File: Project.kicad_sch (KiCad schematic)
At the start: 0 parts

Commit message: 修复晶振画错了的问题
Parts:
- added C1, C2: 1uF, symbol Lib1:C(MM)-LibCool
- added C3: 10uF, symbol Lib1:C(MM)-LibCool
- added C4, C5: 18pF, symbol Lib1:C(MM)-LibCool
- added F1: 20A, symbol Lib1:FUSE*-LibCool
- added P1: USB_C_Plug, symbol Connector:USB_C_Plug
- added R?: 1M, symbol Lib1:RES(M)-LibCool
- added SW1: DOUBLE_KEY, symbol Lib1:DOUBLE_KEY
- added U1: MAX15062A, Package_DFN_QFN:DFN-8_2x2mm_P0.5mm, symbol Regulator_Switching:MAX15062A
- added U2: TUSB8041, Package_DFN_QFN:QFN-64-1EP_9x9mm_P0.5mm_EP6x6mm_ThermalVias, symbol Interface_USB:TUSB8041
- added Y1: 24MHz, symbol Lib1:OSC-LibCool
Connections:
- new net: C2.1, F1.1, P1.A4 (VBUS), P1.A9 (VBUS), P1.B4 (VBUS), P1.B9 (VBUS)
- new net: C1.1, U1.3 (VCC)
- new net: C4.2, R?.2, U2.62 (XI), Y1.1
- new net: C5.2, R?.1, U2.61 (XO), Y1.2
- new net: P1.A1 (GND), P1.A12 (GND), P1.B1 (GND), P1.B12 (GND)
- new net: SW1.1, U2.50 (GRSTz)
- new net +3V3: C3.1, SW1.2, U1.4 (FB/Vout)
- new net GND: C1.2, C2.2, C3.2, C4.1, C5.1, SW1.2, U1.7 (GND)
- new net POWER: F1.2, U1.1 (VIN), U1.2 (EN/UVLO), U2.48 (USB_VBUS)

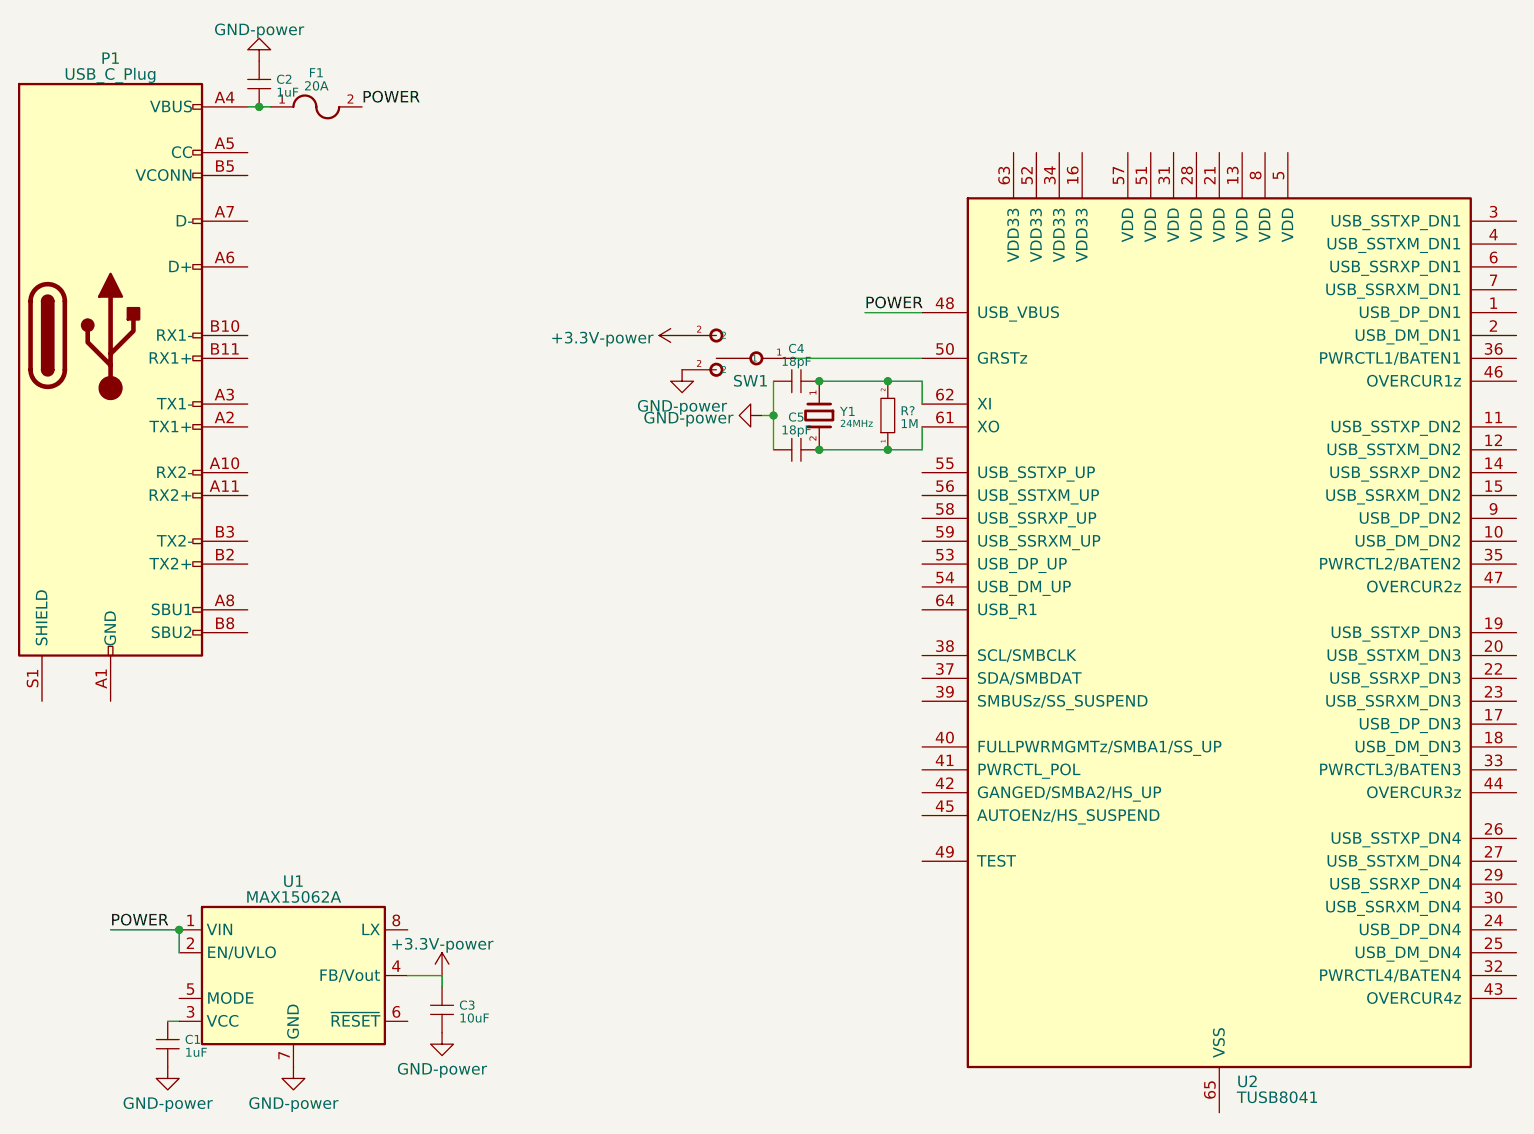
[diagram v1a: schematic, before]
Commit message: 添加信号下拉电阻，修复VBus过压
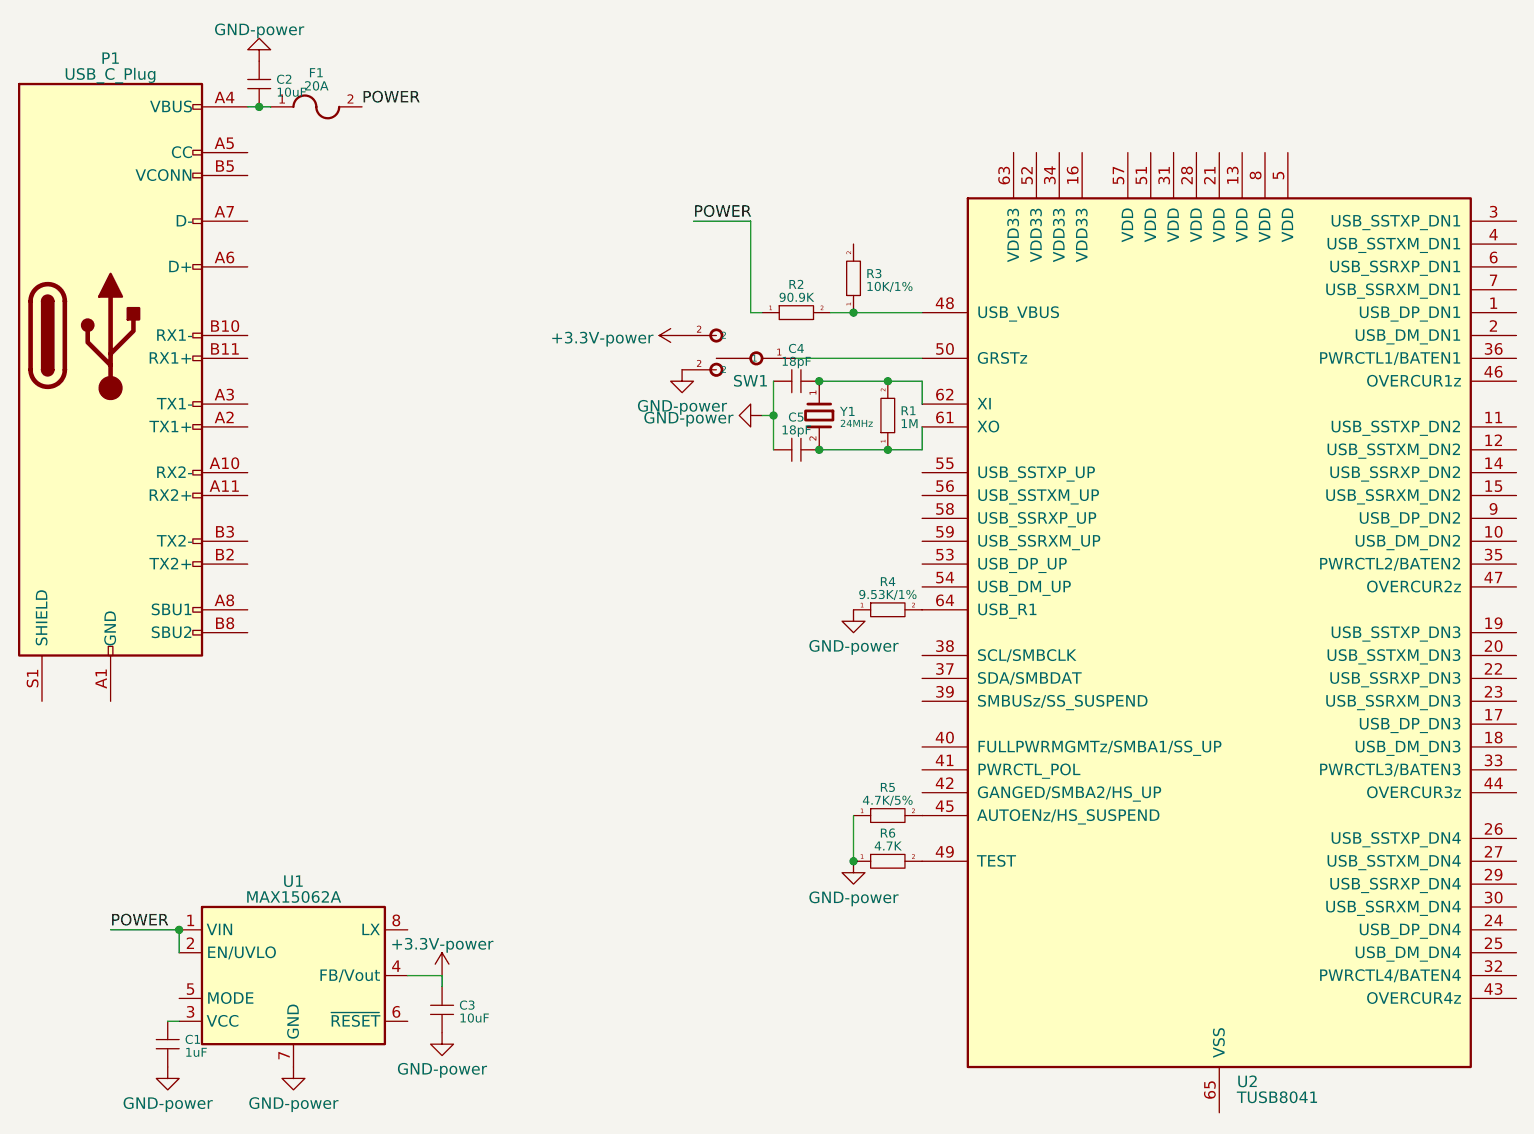
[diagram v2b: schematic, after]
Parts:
- added R2: 90.9K, symbol Lib1:RES(M)-LibCool
- added R3: 10K/1%, symbol Lib1:RES(M)-LibCool
- added R4: 9.53K/1%, symbol Lib1:RES(M)-LibCool
- added R5: 4.7K/5%, symbol Lib1:RES(M)-LibCool
- added R6: 4.7K, symbol Lib1:RES(M)-LibCool
- C2: value 1uF -> 10uF
- gave numbers to parts that had none: 1
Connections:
- net GND: now also R4.1, R5.1, R6.1
- net POWER: now also R2.1; no longer U2.48 (USB_VBUS)
- net at U2.45 (AUTOENz/HS_SUSPEND): now also R5.2
- net at U2.49 (TEST): now also R6.2
- net at U2.64 (USB_R1): now also R4.2
- new net: R2.2, R3.1, U2.48 (USB_VBUS)
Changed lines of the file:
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@@
 (kicad_sch (version 20220126) (generator eeschema)
   (paper "A4")
+  (junction (at 110.49 104.14) (diameter 0) (color 0 0 0 0)
+  )
   (junction (at 101.6 54.61) (diameter 0) (color 0 0 0 0)
   )
+  (junction (at 110.49 43.18) (diameter 0) (color 0 0 0 0)
+  )
   (junction (at 44.45 20.32) (diameter 0) (color 0 0 0 0)
   )
@@
   (junction (at 114.3 58.42) (diameter 0) (color 0 0 0 0)
   )
+  (wire (pts (xy 110.49 43.18) (xy 118.11 43.18))
+    (stroke (width 0) (type default))
+  )
   (wire (pts (xy 114.3 58.42) (xy 118.11 58.42))
     (stroke (width 0) (type default))
@@
     (stroke (width 0) (type default))
   )
-  (wire (pts (xy 111.76 43.18) (xy 118.11 43.18))
+  (wire (pts (xy 92.71 33.02) (xy 99.06 33.02))
+    (stroke (width 0) (type default))
+  )
+  (wire (pts (xy 107.95 43.18) (xy 110.49 43.18))
     (stroke (width 0) (type default))
   )
@@
     (stroke (width 0) (type default))
   )
+  (wire (pts (xy 99.06 33.02) (xy 99.06 43.18))
+    (stroke (width 0) (type default))
+  )
   (wire (pts (xy 101.6 54.61) (xy 101.6 58.42))
     (stroke (width 0) (type default))
@@
     (stroke (width 0) (type default))
   )
+  (wire (pts (xy 99.06 43.18) (xy 100.33 43.18))
+    (stroke (width 0) (type default))
+  )
   (wire (pts (xy 101.6 50.8) (xy 101.6 54.61))
     (stroke (width 0) (type default))
@@
     (stroke (width 0) (type default))
   )
+  (wire (pts (xy 110.49 99.06) (xy 110.49 104.14))
+    (stroke (width 0) (type default))
+  )
   (wire (pts (xy 64.77 116.84) (xy 64.77 118.11))
     (stroke (width 0) (type default))
   )
-  (label "POWER" (at 111.76 43.18 0) (fields_autoplaced)
+  (label "POWER" (at 92.71 33.02 0) (fields_autoplaced)
     (effects (font (size 1.27 1.27)) (justify left bottom))
   )
@@
     (pin "1")
   )
+  (symbol (lib_id "Lib1:RES(M)-LibCool") (at 114.3 76.2 0) (unit 1)
+    (in_bom yes) (on_board yes) (fields_autoplaced)
+    (property "Reference" "R4" (id 0) (at 114.3 73.1046 0)
+      (effects (font (size 0.9906 0.9906)))
+    )
+    (property "Value" "9.53K/1%" (id 1) (at 114.3 74.535 0)
+      (effects (font (size 0.9906 0.9906)))
+    )
+    (property "Footprint" "" (id 2) (at 114.3 76.2 0)
+      (effects (font (size 1.524 1.524)))
+    )
+    (property "Datasheet" "" (id 3) (at 114.3 76.2 0)
+      (effects (font (size 1.524 1.524)))
+    )
+    (pin "1")
+    (pin "2")
+  )
+  (symbol (lib_id "Lib1:RES(M)-LibCool") (at 110.49 39.37 90) (unit 1)
+    (in_bom yes) (on_board yes) (fields_autoplaced)
+    (property "Reference" "R3" (id 0) (at 111.887 38.8784 90)
+      (effects (font (size 0.9906 0.9906)) (justify right))
+    )
+    (property "Value" "10K/1%" (id 1) (at 111.887 40.3088 90)
+      (effects (font (size 0.9906 0.9906)) (justify right))
+    )
+    (property "Footprint" "" (id 2) (at 110.49 39.37 0)
+      (effects (font (size 1.524 1.524)))
+    )
+    (property "Datasheet" "" (id 3) (at 110.49 39.37 0)
+      (effects (font (size 1.524 1.524)))
+    )
+    (pin "1")
+    (pin "2")
+  )
   (symbol (lib_id "Lib1:GND-power") (at 34.29 127 0) (unit 1)
     (in_bom yes) (on_board yes) (fields_autoplaced)
@@
     (pin "1")
   )
+  (symbol (lib_id "Lib1:RES(M)-LibCool") (at 104.14 43.18 0) (unit 1)
+    (in_bom yes) (on_board yes) (fields_autoplaced)
+    (property "Reference" "R2" (id 0) (at 104.14 40.0846 0)
+      (effects (font (size 0.9906 0.9906)))
+    )
+    (property "Value" "90.9K" (id 1) (at 104.14 41.515 0)
+      (effects (font (size 0.9906 0.9906)))
+    )
+    (property "Footprint" "" (id 2) (at 104.14 43.18 0)
+      (effects (font (size 1.524 1.524)))
+    )
+    (property "Datasheet" "" (id 3) (at 104.14 43.18 0)
+      (effects (font (size 1.524 1.524)))
+    )
+    (pin "1")
+    (pin "2")
+  )
   (symbol (lib_id "Lib1:GND-power") (at 91.44 49.53 0) (unit 1)
     (in_bom yes) (on_board yes) (fields_autoplaced)
@@
     (pin "1")
   )
+  (symbol (lib_id "Lib1:GND-power") (at 110.49 76.2 0) (unit 1)
+    (in_bom yes) (on_board yes) (fields_autoplaced)
+    (property "Reference" "#PWR09" (id 0) (at 110.49 82.55 0)
+      (effects (font (size 1.27 1.27)) hide)
+    )
+    (property "Value" "GND-power" (id 1) (at 110.49 80.2561 0)
+      (effects (font (size 1.27 1.27)))
+    )
+    (property "Footprint" "" (id 2) (at 110.49 76.2 0)
+      (effects (font (size 1.27 1.27)) hide)
+    )
+    (property "Datasheet" "" (id 3) (at 110.49 76.2 0)
+      (effects (font (size 1.27 1.27)) hide)
+    )
+    (pin "1")
+  )
   (symbol (lib_id "Lib1:RES(M)-LibCool") (at 114.3 54.61 90) (unit 1)
     (in_bom yes) (on_board yes) (fields_autoplaced)
-    (property "Reference" "R?" (id 0) (at 115.697 54.1184 90)
+    (property "Reference" "R1" (id 0) (at 115.697 54.1184 90)
       (effects (font (size 0.9906 0.9906)) (justify right))
     )
@@
     (pin "2")
   )
+  (symbol (lib_id "Lib1:RES(M)-LibCool") (at 114.3 104.14 0) (unit 1)
+    (in_bom yes) (on_board yes) (fields_autoplaced)
+    (property "Reference" "R6" (id 0) (at 114.3 101.0446 0)
+      (effects (font (size 0.9906 0.9906)))
+    )
+    (property "Value" "4.7K" (id 1) (at 114.3 102.475 0)
+      (effects (font (size 0.9906 0.9906)))
+    )
+    (property "Footprint" "" (id 2) (at 114.3 104.14 0)
+      (effects (font (size 1.524 1.524)))
+    )
+    (property "Datasheet" "" (id 3) (at 114.3 104.14 0)
+      (effects (font (size 1.524 1.524)))
+    )
+    (pin "1")
+    (pin "2")
+  )
   (symbol (lib_id "Lib1:C(MM)-LibCool") (at 44.45 17.78 90) (unit 1)
     (in_bom yes) (on_board yes) (fields_autoplaced)
@@
       (effects (font (size 0.9906 0.9906)) (justify right))
     )
-    (property "Value" "1uF" (id 1) (at 46.355 18.7188 90)
+    (property "Value" "10uF" (id 1) (at 46.355 18.7188 90)
       (effects (font (size 0.9906 0.9906)) (justify right))
     )
@@
     (pin "2")
   )
+  (symbol (lib_id "Lib1:RES(M)-LibCool") (at 114.3 99.06 0) (unit 1)
+    (in_bom yes) (on_board yes) (fields_autoplaced)
+    (property "Reference" "R5" (id 0) (at 114.3 95.9646 0)
+      (effects (font (size 0.9906 0.9906)))
+    )
+    (property "Value" "4.7K/5%" (id 1) (at 114.3 97.395 0)
+      (effects (font (size 0.9906 0.9906)))
+    )
+    (property "Footprint" "" (id 2) (at 114.3 99.06 0)
+      (effects (font (size 1.524 1.524)))
+    )
+    (property "Datasheet" "" (id 3) (at 114.3 99.06 0)
+      (effects (font (size 1.524 1.524)))
+    )
+    (pin "1")
+    (pin "2")
+  )
   (symbol (lib_id "Lib1:+3.3V-power") (at 64.77 116.84 0) (unit 1)
     (in_bom yes) (on_board yes) (fields_autoplaced)
@@
     (pin "1")
     (pin "2")
+  )
+  (symbol (lib_id "Lib1:GND-power") (at 110.49 104.14 0) (unit 1)
+    (in_bom yes) (on_board yes) (fields_autoplaced)
+    (property "Reference" "#PWR010" (id 0) (at 110.49 110.49 0)
+      (effects (font (size 1.27 1.27)) hide)
+    )
+    (property "Value" "GND-power" (id 1) (at 110.49 108.1961 0)
+      (effects (font (size 1.27 1.27)))
+    )
+    (property "Footprint" "" (id 2) (at 110.49 104.14 0)
+      (effects (font (size 1.27 1.27)) hide)
+    )
+    (property "Datasheet" "" (id 3) (at 110.49 104.14 0)
+      (effects (font (size 1.27 1.27)) hide)
+    )
+    (pin "1")
   )
   (sheet_instances
@@
       (reference "#PWR08") (unit 1) (value "GND-power") (footprint "")
     )
+    (path "/5a854202-96c4-4452-a2e1-9a4e2d5a9daa"
+      (reference "#PWR09") (unit 1) (value "GND-power") (footprint "")
+    )
+    (path "/de51df0a-3dcd-43da-a83f-ddf46ab858ea"
+      (reference "#PWR010") (unit 1) (value "GND-power") (footprint "")
+    )
     (path "/1af607d6-b127-45ad-990a-6c742ba65adb"
       (reference "C1") (unit 1) (value "1uF") (footprint "")
     )
     (path "/afd003d5-9c29-4e6f-a874-c9df81b8919a"
-      (reference "C2") (unit 1) (value "1uF") (footprint "")
+      (reference "C2") (unit 1) (value "10uF") (footprint "")
     )
     (path "/db333850-3d38-4e49-bcfe-e1113a3d7c1e"
@@
     )
     (path "/5ea86072-a7e8-4217-b89a-0b5f823257e6"
-      (reference "R?") (unit 1) (value "1M") (footprint "")
+      (reference "R1") (unit 1) (value "1M") (footprint "")
+    )
+    (path "/55fb820b-b139-408a-b156-e0fed4ea26f1"
+      (reference "R2") (unit 1) (value "90.9K") (footprint "")
+    )
+    (path "/31149060-8946-4746-90d6-cb0eed87aa91"
+      (reference "R3") (unit 1) (value "10K/1%") (footprint "")
+    )
+    (path "/275bb50f-8e2a-413d-9ba3-f1dbd0f276db"
+      (reference "R4") (unit 1) (value "9.53K/1%") (footprint "")
+    )
+    (path "/d48211d6-1156-463b-8cf5-ee4a4148a68f"
+      (reference "R5") (unit 1) (value "4.7K/5%") (footprint "")
+    )
+    (path "/91943703-cb01-41c6-8e90-e8941679b170"
+      (reference "R6") (unit 1) (value "4.7K") (footprint "")
     )
     (path "/6fe75d49-764d-49bf-bc4c-ca066962e8aa"
